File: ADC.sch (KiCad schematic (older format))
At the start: 4 parts

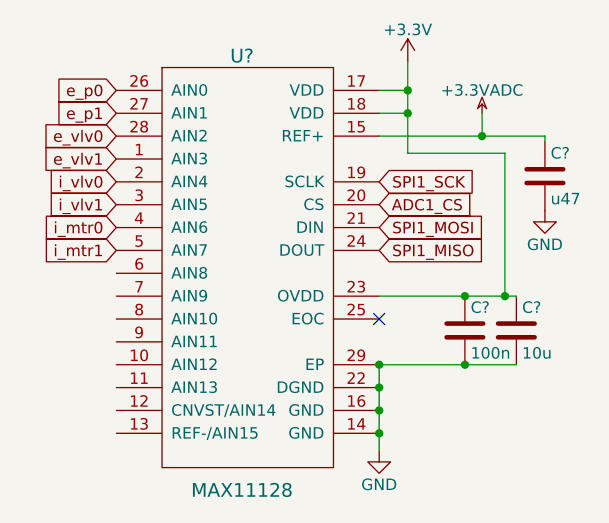
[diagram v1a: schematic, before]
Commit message: Eletrical Rules Check
Fixed some label names
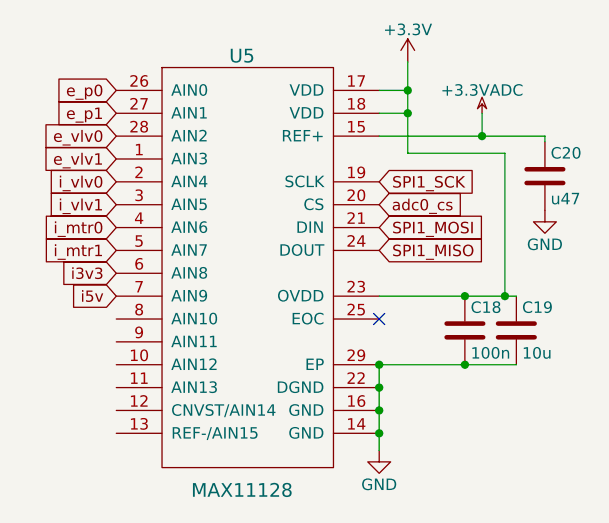
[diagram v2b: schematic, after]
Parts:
- gave numbers to parts that had none: 4
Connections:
- net i3v3: now reaches U5.6 (AIN8)
- net i5v: now reaches U5.7 (AIN9)
- net ADC1_CS renamed adc0_cs
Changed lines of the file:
@@
 AR Path="/596D7A67/5C1804A3/5E64F4D7" Ref="U?"  Part="1"
 AR Path="/5E49E893/5E64F4D7" Ref="U?"  Part="1"
-AR Path="/5E63996E/5E64F4D7" Ref="U?"  Part="1"
-F 0 "U?" H 5325 3850 60  0000 C CNN
+AR Path="/5E63996E/5E64F4D7" Ref="U5"  Part="1"
+F 0 "U5" H 5325 3850 60  0000 C CNN
 F 1 "MAX11128" H 5325 1950 60  0000 C CNN
 F 2 "sternie:TQFN-28" H 4775 3400 60  0001 C CNN
@@
 AR Path="/596D7A67/5C1804A3/5E64F4DD" Ref="#PWR?"  Part="1"
 AR Path="/5E49E893/5E64F4DD" Ref="#PWR?"  Part="1"
-AR Path="/5E63996E/5E64F4DD" Ref="#PWR?"  Part="1"
-F 0 "#PWR?" H 6525 2450 50  0001 C CNN
+AR Path="/5E63996E/5E64F4DD" Ref="#PWR050"  Part="1"
+F 0 "#PWR050" H 6525 2450 50  0001 C CNN
 F 1 "+3.3VADC" H 6375 2600 50  0000 C CNN
 F 2 "" H 6375 2500 50  0001 C CNN
@@
 AR Path="/596D7A67/5C1804A3/5E64F4E3" Ref="#PWR?"  Part="1"
 AR Path="/5E49E893/5E64F4E3" Ref="#PWR?"  Part="1"
-AR Path="/5E63996E/5E64F4E3" Ref="#PWR?"  Part="1"
-F 0 "#PWR?" H 6050 2125 50  0001 C CNN
+AR Path="/5E63996E/5E64F4E3" Ref="#PWR049"  Part="1"
+F 0 "#PWR049" H 6050 2125 50  0001 C CNN
 F 1 "+3.3V" H 6050 2415 50  0000 C CNN
 F 2 "" H 6050 2275 50  0001 C CNN
@@
 AR Path="/596D7A67/5C1804A3/5E64F4E9" Ref="C?"  Part="1"
 AR Path="/5E49E893/5E64F4E9" Ref="C?"  Part="1"
-AR Path="/5E63996E/5E64F4E9" Ref="C?"  Part="1"
-F 0 "C?" H 6675 2875 50  0000 L CNN
+AR Path="/5E63996E/5E64F4E9" Ref="C20"  Part="1"
+F 0 "C20" H 6675 2875 50  0000 L CNN
 F 1 "u47" H 6675 2675 50  0000 L CNN
 F 2 "Capacitors_SMD:C_0603" H 6688 2625 50  0001 C CNN
@@
 AR Path="/596D7A67/5C1804A3/5E64F4EF" Ref="#PWR?"  Part="1"
 AR Path="/5E49E893/5E64F4EF" Ref="#PWR?"  Part="1"
-AR Path="/5E63996E/5E64F4EF" Ref="#PWR?"  Part="1"
-F 0 "#PWR?" H 6650 2675 50  0001 C CNN
+AR Path="/5E63996E/5E64F4EF" Ref="#PWR051"  Part="1"
+F 0 "#PWR051" H 6650 2675 50  0001 C CNN
 F 1 "GND" H 6650 2775 50  0000 C CNN
 F 2 "" H 6650 2925 50  0001 C CNN
@@
 AR Path="/596D7A67/5C1804A3/5E64F4F5" Ref="#PWR?"  Part="1"
 AR Path="/5E49E893/5E64F4F5" Ref="#PWR?"  Part="1"
-AR Path="/5E63996E/5E64F4F5" Ref="#PWR?"  Part="1"
-F 0 "#PWR?" H 5925 3725 50  0001 C CNN
+AR Path="/5E63996E/5E64F4F5" Ref="#PWR048"  Part="1"
+F 0 "#PWR048" H 5925 3725 50  0001 C CNN
 F 1 "GND" H 5925 3825 50  0000 C CNN
 F 2 "" H 5925 3975 50  0001 C CNN
@@
 AR Path="/596D7A67/5C1804A3/5E64F4FB" Ref="C?"  Part="1"
 AR Path="/5E49E893/5E64F4FB" Ref="C?"  Part="1"
-AR Path="/5E63996E/5E64F4FB" Ref="C?"  Part="1"
-F 0 "C?" H 6325 3550 50  0000 L CNN
+AR Path="/5E63996E/5E64F4FB" Ref="C18"  Part="1"
+F 0 "C18" H 6325 3550 50  0000 L CNN
 F 1 "100n" H 6325 3350 50  0000 L CNN
 F 2 "Capacitors_SMD:C_0603" H 6338 3300 50  0001 C CNN
@@
 AR Path="/596D7A67/5C1804A3/5E64F501" Ref="C?"  Part="1"
 AR Path="/5E49E893/5E64F501" Ref="C?"  Part="1"
-AR Path="/5E63996E/5E64F501" Ref="C?"  Part="1"
-F 0 "C?" H 6550 3550 50  0000 L CNN
+AR Path="/5E63996E/5E64F501" Ref="C19"  Part="1"
+F 0 "C19" H 6550 3550 50  0000 L CNN
 F 1 "10u" H 6550 3350 50  0000 L CNN
 F 2 "Capacitors_SMD:C_0805" H 6563 3300 50  0001 C CNN
@@
 	6475 3300 6525 3300
 Text GLabel 5925 2900 2    49   Input ~ 0
-ADC1_CS
+adc0_cs
 Connection ~ 5925 3600
 Text GLabel 4775 2400 0    50   Input ~ 0
@@
 Text GLabel 5925 2800 2    50   Input ~ 0
 SPI1_SCK
+Text GLabel 4775 3200 0    49   Input ~ 0
+i3v3
+Text GLabel 4775 3300 0    49   Input ~ 0
+i5v
 $EndSCHEMATC
